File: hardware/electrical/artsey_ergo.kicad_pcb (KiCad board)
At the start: 2 copper layers, 94 x 57.8 mm, 29 parts, among them CN1 JST PH 2.0mm 1x2, K1 Kailh Choc Hotswap, K2 Kailh Choc Hotswap, K3 Kailh Choc Hotswap, K4 Kailh Choc Hotswap, K5 Kailh Choc Hotswap, K6 Kailh Choc Hotswap, K7 Kailh Choc Hotswap, K8 Kailh Choc Hotswap, SW1 Alps SSSS811101

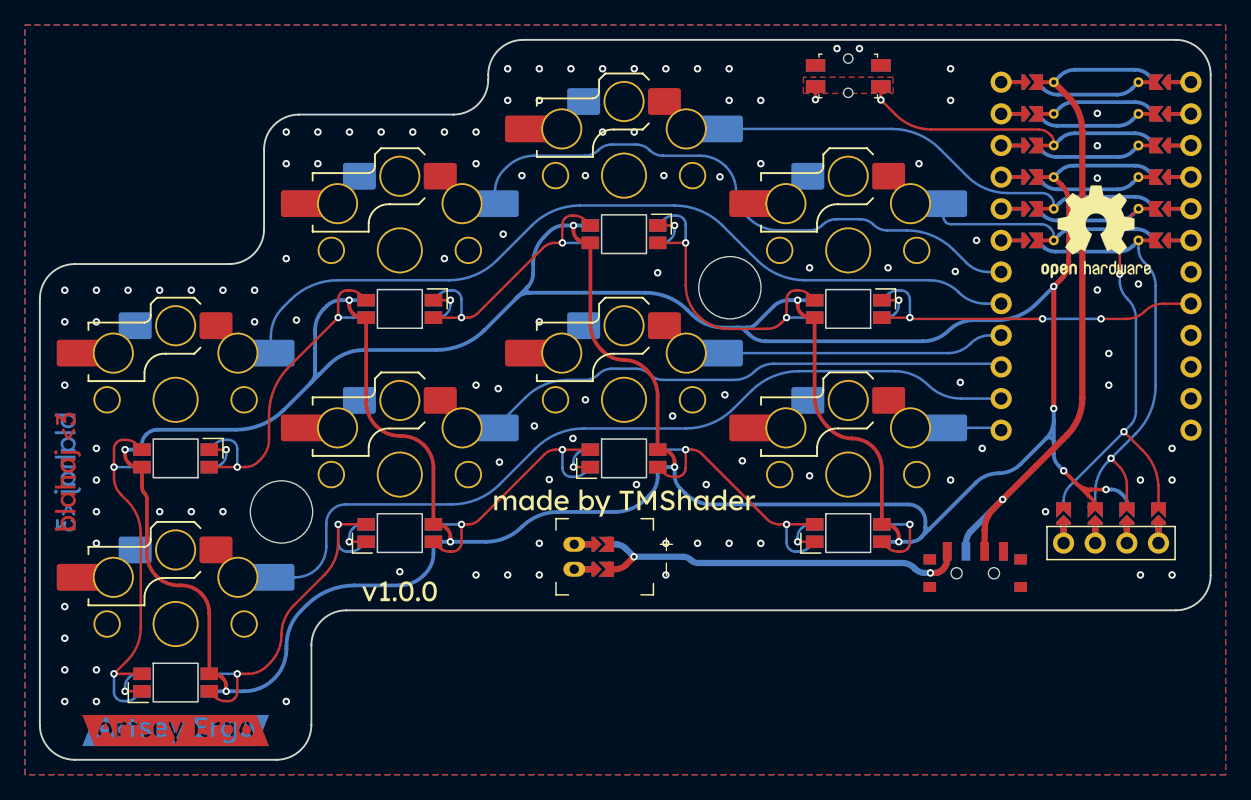
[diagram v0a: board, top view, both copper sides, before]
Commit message: Add panelized JLCPCB build, make actions faster by skipping rendering with a variable
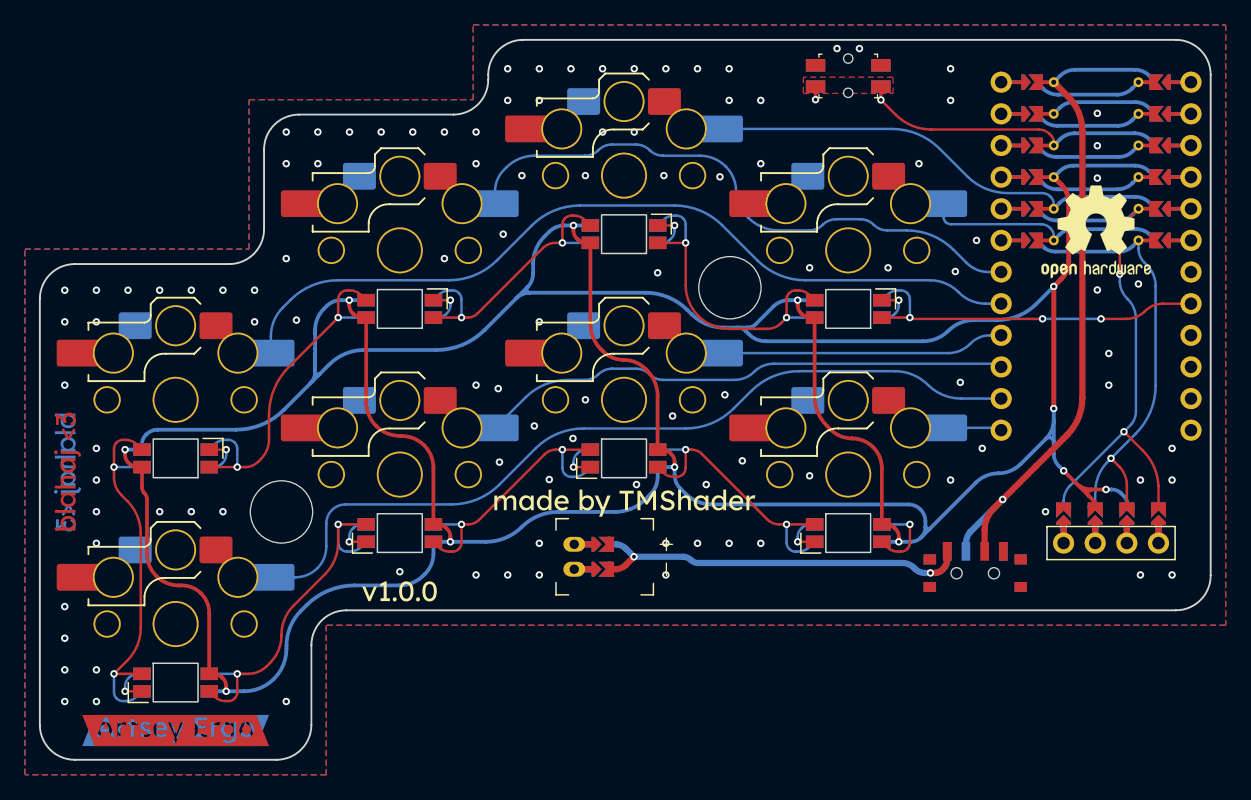
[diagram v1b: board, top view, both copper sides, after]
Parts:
- added OL1: Value, Artsey_Ergo:Outline, F.Cu at (148.5, 105.0)
- added REF**: Tab, PCM_kikit:Tab, F.Cu at (110.6, 94.1)
- added REF**: Tab, PCM_kikit:Tab, F.Cu at (186.3, 121.9)
- added REF**: Tab, PCM_kikit:Tab, F.Cu at (148.5, 121.9)
- added REF**: Tab, PCM_kikit:Tab, F.Cu at (112.5, 133.9)
- added REF**: Tab, PCM_kikit:Tab, F.Cu at (148.5, 76.1)
- added REF**: Tab, PCM_kikit:Tab, F.Cu at (186.3, 76.1)
